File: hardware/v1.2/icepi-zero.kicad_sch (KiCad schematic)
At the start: 29 parts, among them J1 Conn_02x20_Counter_Clockwise, SW1 SW_Push, SW2 SW_Push, U1 ECP5U_25F_CABGA256, Y1 SITxxxxxx-1x-33E-50.000000

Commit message: Trying to document my journey :)
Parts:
- renumbered C25 to C1, C1 to C2, C2 to C3
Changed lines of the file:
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@@
 		(dnp no)
 		(fields_autoplaced yes)
-		(property "Reference" "#PWR013"
+		(property "Reference" "#PWR015"
 			(at 123.19 106.68 0)
 			(effects
@@
 			(project "icepi-zero"
 				(path "/f88da08e-cf42-4d03-a08f-3f602fe6658d"
-					(reference "#PWR013")
+					(reference "#PWR015")
 					(unit 1)
 				)
@@
 		(dnp no)
 		(fields_autoplaced yes)
-		(property "Reference" "#PWR020"
+		(property "Reference" "#PWR022"
 			(at 123.19 144.78 0)
 			(effects
@@
 			(project "icepi-zero"
 				(path "/f88da08e-cf42-4d03-a08f-3f602fe6658d"
-					(reference "#PWR020")
+					(reference "#PWR022")
 					(unit 1)
 				)
@@
 		(dnp no)
 		(fields_autoplaced yes)
-		(property "Reference" "#PWR021"
+		(property "Reference" "#PWR023"
 			(at 223.52 156.21 0)
 			(effects
@@
 			(project ""
 				(path "/f88da08e-cf42-4d03-a08f-3f602fe6658d"
-					(reference "#PWR021")
+					(reference "#PWR023")
 					(unit 1)
 				)
@@
 		(dnp no)
 		(fields_autoplaced yes)
-		(property "Reference" "#PWR016"
+		(property "Reference" "#PWR018"
 			(at 148.59 119.38 0)
 			(effects
@@
 			(project "icepi-zero"
 				(path "/f88da08e-cf42-4d03-a08f-3f602fe6658d"
-					(reference "#PWR016")
+					(reference "#PWR018")
 					(unit 1)
 				)
@@
 		(dnp no)
 		(fields_autoplaced yes)
-		(property "Reference" "#PWR017"
+		(property "Reference" "#PWR019"
 			(at 123.19 127 0)
 			(effects
@@
 			(project "icepi-zero"
 				(path "/f88da08e-cf42-4d03-a08f-3f602fe6658d"
-					(reference "#PWR017")
+					(reference "#PWR019")
 					(unit 1)
 				)
@@
 		(dnp no)
 		(fields_autoplaced yes)
-		(property "Reference" "#PWR011"
+		(property "Reference" "#PWR013"
 			(at 138.43 99.06 0)
 			(effects
@@
 			(project ""
 				(path "/f88da08e-cf42-4d03-a08f-3f602fe6658d"
-					(reference "#PWR011")
+					(reference "#PWR013")
 					(unit 1)
 				)
@@
 		(dnp no)
 		(fields_autoplaced yes)
-		(property "Reference" "#PWR05"
+		(property "Reference" "#PWR07"
 			(at 247.65 62.23 0)
 			(effects
@@
 			(project ""
 				(path "/f88da08e-cf42-4d03-a08f-3f602fe6658d"
-					(reference "#PWR05")
+					(reference "#PWR07")
 					(unit 1)
 				)
@@
 		(dnp no)
 		(fields_autoplaced yes)
-		(property "Reference" "#PWR09"
+		(property "Reference" "#PWR011"
 			(at 133.35 96.52 0)
 			(effects
@@
 			(project ""
 				(path "/f88da08e-cf42-4d03-a08f-3f602fe6658d"
-					(reference "#PWR09")
+					(reference "#PWR011")
 					(unit 1)
 				)
@@
 		(dnp no)
 		(fields_autoplaced yes)
-		(property "Reference" "C1"
+		(property "Reference" "C2"
 			(at 29.21 81.2862 0)
 			(effects
@@
 			(project "icepi-zero"
 				(path "/f88da08e-cf42-4d03-a08f-3f602fe6658d"
-					(reference "C1")
+					(reference "C2")
 					(unit 1)
 				)
@@
 		(dnp no)
 		(fields_autoplaced yes)
-		(property "Reference" "#PWR019"
+		(property "Reference" "#PWR021"
 			(at 148.59 137.16 0)
 			(effects
@@
 			(project "icepi-zero"
 				(path "/f88da08e-cf42-4d03-a08f-3f602fe6658d"
-					(reference "#PWR019")
+					(reference "#PWR021")
 					(unit 1)
 				)
@@
 		(dnp no)
 		(fields_autoplaced yes)
-		(property "Reference" "#PWR044"
+		(property "Reference" "#PWR04"
 			(at 43.18 62.23 0)
 			(effects
@@
 			(project "icepi-zero"
 				(path "/f88da08e-cf42-4d03-a08f-3f602fe6658d"
-					(reference "#PWR044")
+					(reference "#PWR04")
 					(unit 1)
 				)
@@
 		(dnp no)
 		(fields_autoplaced yes)
-		(property "Reference" "#PWR06"
+		(property "Reference" "#PWR08"
 			(at 257.81 62.23 0)
 			(effects
@@
 			(project ""
 				(path "/f88da08e-cf42-4d03-a08f-3f602fe6658d"
-					(reference "#PWR06")
+					(reference "#PWR08")
 					(unit 1)
 				)
@@
 		(dnp no)
 		(fields_autoplaced yes)
-		(property "Reference" "#PWR022"
+		(property "Reference" "#PWR024"
 			(at 142.24 185.42 0)
 			(effects
@@
 			(project ""
 				(path "/f88da08e-cf42-4d03-a08f-3f602fe6658d"
-					(reference "#PWR022")
+					(reference "#PWR024")
 					(unit 1)
 				)
@@
 		(dnp no)
 		(fields_autoplaced yes)
-		(property "Reference" "#PWR043"
+		(property "Reference" "#PWR01"
 			(at 43.18 41.91 0)
 			(effects
@@
 			(project "icepi-zero"
 				(path "/f88da08e-cf42-4d03-a08f-3f602fe6658d"
-					(reference "#PWR043")
+					(reference "#PWR01")
 					(unit 1)
 				)
@@
 		(dnp no)
 		(fields_autoplaced yes)
-		(property "Reference" "#PWR08"
+		(property "Reference" "#PWR010"
 			(at 36.83 92.71 0)
 			(effects
@@
 			(project "icepi-zero"
 				(path "/f88da08e-cf42-4d03-a08f-3f602fe6658d"
-					(reference "#PWR08")
+					(reference "#PWR010")
 					(unit 1)
 				)
@@
 		(dnp no)
 		(fields_autoplaced yes)
-		(property "Reference" "C2"
+		(property "Reference" "C3"
 			(at 39.37 81.2862 0)
 			(effects
@@
 			(project "icepi-zero"
 				(path "/f88da08e-cf42-4d03-a08f-3f602fe6658d"
-					(reference "C2")
+					(reference "C3")
 					(unit 1)
 				)
@@
 		(dnp no)
 		(fields_autoplaced yes)
-		(property "Reference" "#PWR07"
+		(property "Reference" "#PWR09"
 			(at 24.13 81.28 0)
 			(effects
@@
 			(project "icepi-zero"
 				(path "/f88da08e-cf42-4d03-a08f-3f602fe6658d"
-					(reference "#PWR07")
+					(reference "#PWR09")
 					(unit 1)
 				)
@@
 		(dnp no)
 		(fields_autoplaced yes)
-		(property "Reference" "#PWR010"
+		(property "Reference" "#PWR012"
 			(at 138.43 96.52 0)
 			(effects
@@
 			(project "icepi-zero"
 				(path "/f88da08e-cf42-4d03-a08f-3f602fe6658d"
-					(reference "#PWR010")
+					(reference "#PWR012")
 					(unit 1)
 				)
@@
 		(on_board yes)
 		(dnp no)
-		(property "Reference" "C25"
+		(property "Reference" "C1"
 			(at 28.575 45.72 0)
 			(effects
@@
 			(project "icepi-zero"
 				(path "/f88da08e-cf42-4d03-a08f-3f602fe6658d"
-					(reference "C25")
+					(reference "C1")
 					(unit 1)
 				)
@@
 		(dnp no)
 		(fields_autoplaced yes)
-		(property "Reference" "#PWR04"
+		(property "Reference" "#PWR06"
 			(at 236.22 62.23 0)
 			(effects
@@
 			(project ""
 				(path "/f88da08e-cf42-4d03-a08f-3f602fe6658d"
-					(reference "#PWR04")
+					(reference "#PWR06")
 					(unit 1)
 				)
@@
 		(dnp no)
 		(fields_autoplaced yes)
-		(property "Reference" "#PWR01"
+		(property "Reference" "#PWR02"
 			(at 236.22 49.53 0)
 			(effects
@@
 			(project ""
 				(path "/f88da08e-cf42-4d03-a08f-3f602fe6658d"
-					(reference "#PWR01")
+					(reference "#PWR02")
 					(unit 1)
 				)
@@
 		(dnp no)
 		(fields_autoplaced yes)
-		(property "Reference" "#PWR012"
+		(property "Reference" "#PWR014"
 			(at 148.59 101.6 0)
 			(effects
@@
 			(project ""
 				(path "/f88da08e-cf42-4d03-a08f-3f602fe6658d"
-					(reference "#PWR012")
+					(reference "#PWR014")
 					(unit 1)
 				)
@@
 		(dnp no)
 		(fields_autoplaced yes)
-		(property "Reference" "#PWR018"
+		(property "Reference" "#PWR020"
 			(at 148.59 132.08 0)
 			(effects
@@
 			(project "icepi-zero"
 				(path "/f88da08e-cf42-4d03-a08f-3f602fe6658d"
-					(reference "#PWR018")
+					(reference "#PWR020")
 					(unit 1)
 				)
@@
 		(dnp no)
 		(fields_autoplaced yes)
-		(property "Reference" "#PWR02"
+		(property "Reference" "#PWR03"
 			(at 247.65 49.53 0)
 			(effects
@@
 			(project ""
 				(path "/f88da08e-cf42-4d03-a08f-3f602fe6658d"
-					(reference "#PWR02")
+					(reference "#PWR03")
 					(unit 1)
 				)
@@
 		(dnp no)
 		(fields_autoplaced yes)
-		(property "Reference" "#PWR015"
+		(property "Reference" "#PWR017"
 			(at 133.35 116.84 0)
 			(effects
@@
 			(project "icepi-zero"
 				(path "/f88da08e-cf42-4d03-a08f-3f602fe6658d"
-					(reference "#PWR015")
+					(reference "#PWR017")
 					(unit 1)
 				)
@@
 		(dnp no)
 		(fields_autoplaced yes)
-		(property "Reference" "#PWR03"
+		(property "Reference" "#PWR05"
 			(at 226.06 62.23 0)
 			(effects
@@
 			(project ""
 				(path "/f88da08e-cf42-4d03-a08f-3f602fe6658d"
-					(reference "#PWR03")
+					(reference "#PWR05")
 					(unit 1)
 				)
@@
 		(dnp no)
 		(fields_autoplaced yes)
-		(property "Reference" "#PWR014"
+		(property "Reference" "#PWR016"
 			(at 148.59 111.76 0)
 			(effects
@@
 			(project "icepi-zero"
 				(path "/f88da08e-cf42-4d03-a08f-3f602fe6658d"
-					(reference "#PWR014")
+					(reference "#PWR016")
 					(unit 1)
 				)

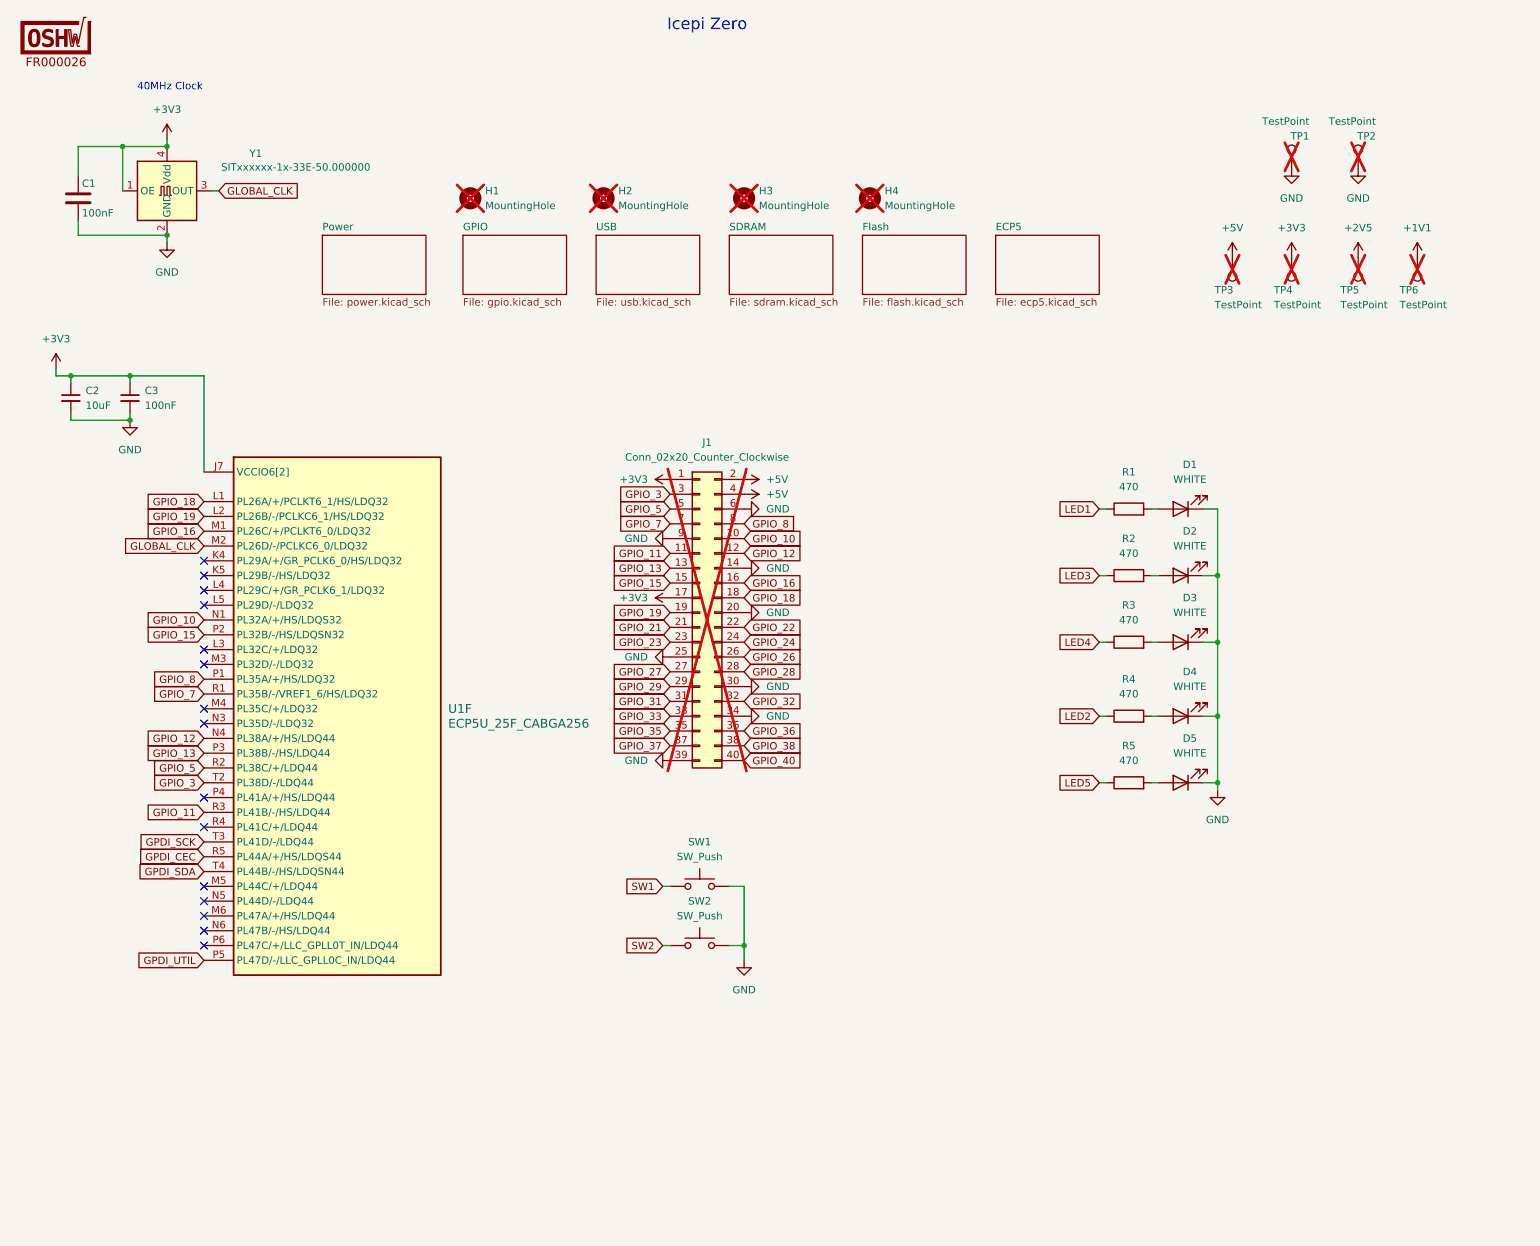
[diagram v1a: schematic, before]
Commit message: Custom ECP5-CABGA256 symbol
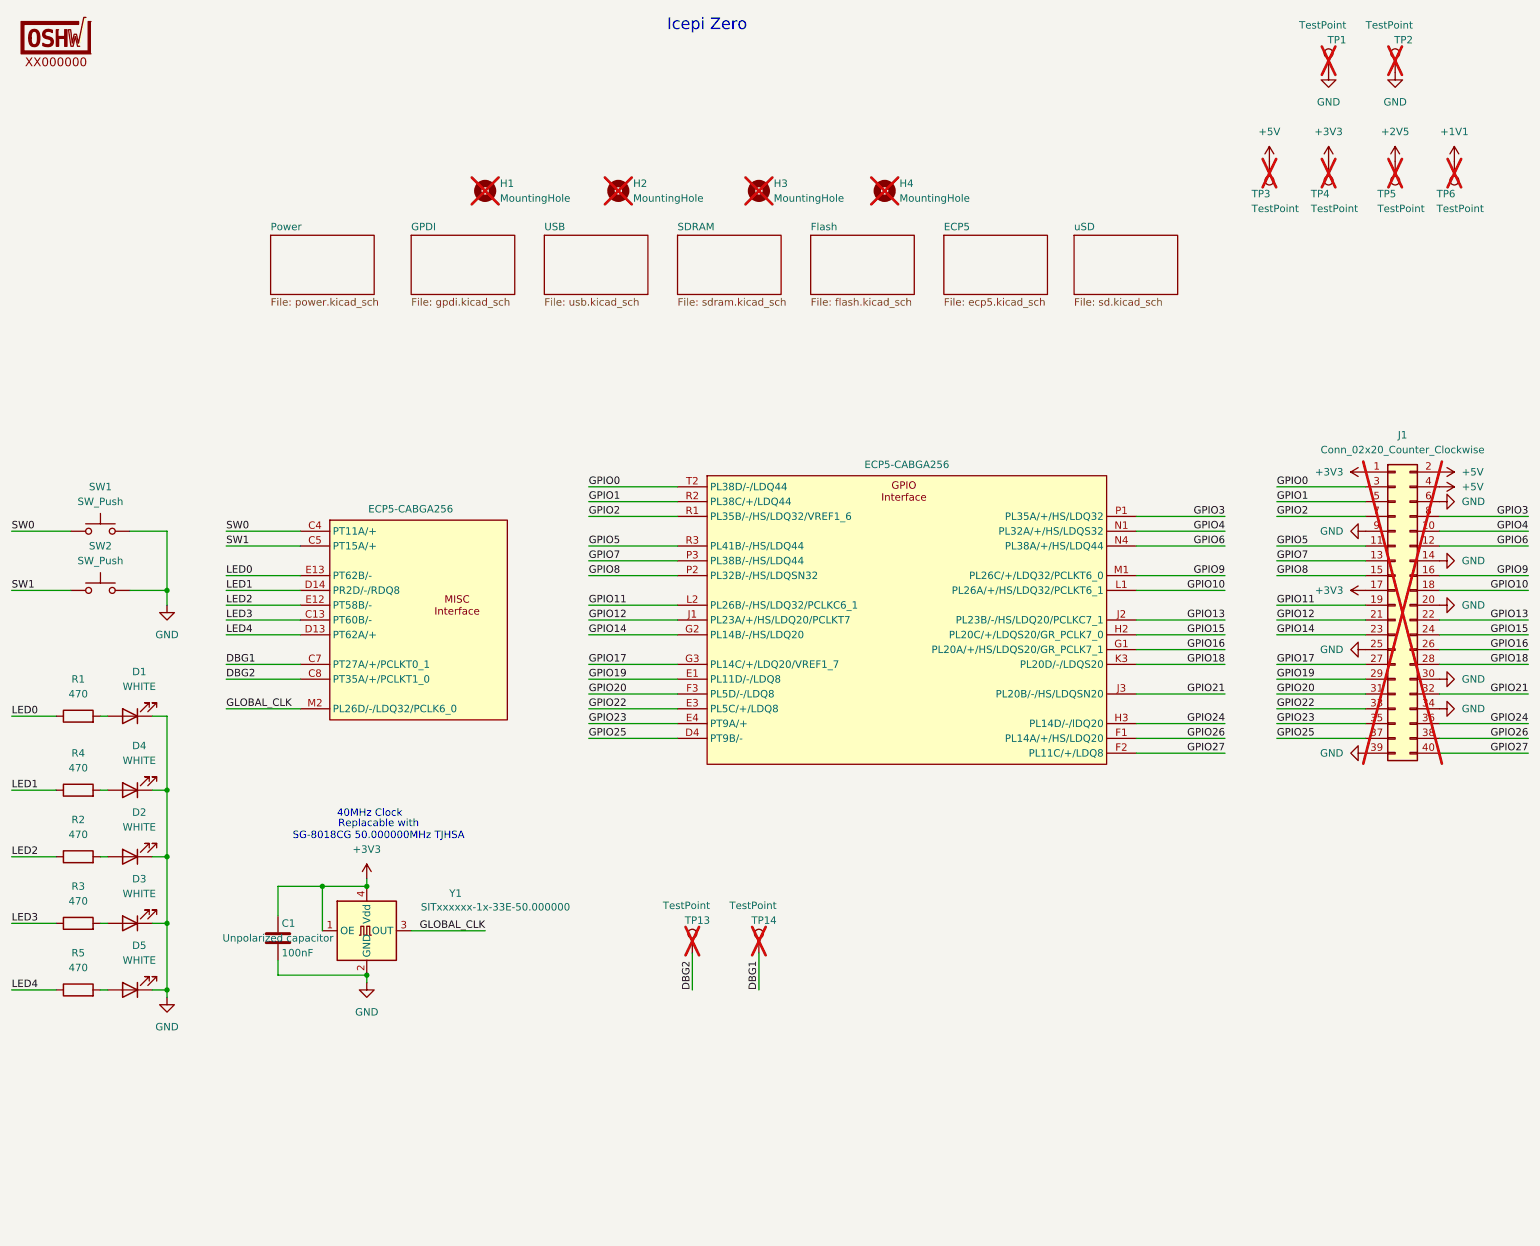
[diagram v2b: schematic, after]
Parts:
- removed C2: 10uF, Capacitor_SMD:C_0603_1608Metric, symbol Device:C_Small
- removed C3: 100nF, Capacitor_SMD:C_0402_1005Metric, symbol Device:C_Small
- removed U1: ECP5U_25F_CABGA256, Package_BGA:BGA-256_14.0x14.0mm_Layout16x16_P0.8mm_Ball0.45mm_Pad0.32mm_NSMD, symbol josh:ECP5U_12_CABGA256
- added TP13, TP14: TestPoint, TestPoint:TestPoint_Pad_D1.0mm, symbol Connector:TestPoint
- added U1: ECP5-CABGA256, Package_BGA:BGA-256_14.0x14.0mm_Layout16x16_P0.8mm_Ball0.45mm_Pad0.32mm_NSMD, symbol icepi-lib:LFE5U-25F-6BG256x
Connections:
- net LED5 is gone; now on net LED4: R5.1
- net SW2 is gone; now on net SW1: SW2.1
- net GLOBAL_CLK: now also U1.M2 (PL26D/-/LDQ32/PCLK6_0)
- net LED1: now also R4.1, U1.D14 (PR2D/-/RDQ8); no longer R1.1
- net LED2: now also R2.1, U1.E12 (PT58B/-); no longer R4.1
- net LED3: now also R3.1, U1.C13 (PT60B/-); no longer R2.1
- net LED4: now also U1.D13 (PT62A/+); no longer R3.1
- net SW1: now also U1.C5 (PT15A/+); no longer SW1.1
- net GPIO_10 renamed GPIO4
- net GPIO4: now also U1.N1 (PL32A/+/HS/LDQS32)
- net GPIO_11 renamed GPIO5
- net GPIO5: now also U1.R3 (PL41B/-/HS/LDQ44)
- net GPIO_12 renamed GPIO6
- net GPIO6: now also U1.N4 (PL38A/+/HS/LDQ44)
- net GPIO_13 renamed GPIO7
- net GPIO7: now also U1.P3 (PL38B/-/HS/LDQ44)
- net GPIO_15 renamed GPIO8
- net GPIO8: now also U1.P2 (PL32B/-/HS/LDQSN32)
- net GPIO_16 renamed GPIO9
- net GPIO9: now also U1.M1 (PL26C/+/LDQ32/PCLKT6_0)
- net GPIO_18 renamed GPIO10
- net GPIO10: now also U1.L1 (PL26A/+/HS/LDQ32/PCLKT6_1)
- net GPIO_19 renamed GPIO11
- net GPIO11: now also U1.L2 (PL26B/-/HS/LDQ32/PCLKC6_1)
- net GPIO_21 renamed GPIO12
- net GPIO12: now also U1.J1 (PL23A/+/HS/LDQ20/PCLKT7)
- net GPIO_22 renamed GPIO13
- net GPIO13: now also U1.J2 (PL23B/-/HS/LDQ20/PCLKC7_1)
- net GPIO_23 renamed GPIO14
- net GPIO14: now also U1.G2 (PL14B/-/HS/LDQ20)
- net GPIO_24 renamed GPIO15
- net GPIO15: now also U1.H2 (PL20C/+/LDQS20/GR_PCLK7_0)
- net GPIO_26 renamed GPIO16
- net GPIO16: now also U1.G1 (PL20A/+/HS/LDQS20/GR_PCLK7_1)
- net GPIO_27 renamed GPIO17
- net GPIO17: now also U1.G3 (PL14C/+/LDQ20/VREF1_7)
- net GPIO_28 renamed GPIO18
- net GPIO18: now also U1.K3 (PL20D/-/LDQS20)
- net GPIO_29 renamed GPIO19
- net GPIO19: now also U1.E1 (PL11D/-/LDQ8)
- net GPIO_3 renamed GPIO0
- net GPIO0: now also U1.T2 (PL38D/-/LDQ44)
- net GPIO_31 renamed GPIO20
- net GPIO20: now also U1.F3 (PL5D/-/LDQ8)
- net GPIO_32 renamed GPIO21
- net GPIO21: now also U1.J3 (PL20B/-/HS/LDQSN20)
- net GPIO_33 renamed GPIO22
- net GPIO22: now also U1.E3 (PL5C/+/LDQ8)
- net GPIO_35 renamed GPIO23
- net GPIO23: now also U1.E4 (PT9A/+)
- net GPIO_36 renamed GPIO24
- net GPIO24: now also U1.H3 (PL14D/-/lDQ20)
- net GPIO_37 renamed GPIO25
- net GPIO25: now also U1.D4 (PT9B/-)
- net GPIO_38 renamed GPIO26
- net GPIO26: now also U1.F1 (PL14A/+/HS/LDQ20)
- net GPIO_40 renamed GPIO27
- net GPIO27: now also U1.F2 (PL11C/+/LDQ8)
- net GPIO_5 renamed GPIO1
- net GPIO1: now also U1.R2 (PL38C/+/LDQ44)
- net GPIO_7 renamed GPIO2
- net GPIO2: now also U1.R1 (PL35B/-/HS/LDQ32/VREF1_6)
- net GPIO_8 renamed GPIO3
- net GPIO3: now also U1.P1 (PL35A/+/HS/LDQ32)
- new net DBG1: TP14.1, U1.C7 (PT27A/+/PCLKT0_1)
- new net DBG2: TP13.1, U1.C8 (PT35A/+/PCLKT1_0)
- new net LED0: R1.1, U1.E13 (PT62B/-)
- new net SW0: SW1.1, U1.C4 (PT11A/+)
- no-connect marks 15 -> 0
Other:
- sheet GPIO renamed GPDI
- added sheet uSD (sd.kicad_sch)
- sheet GPDI: file gpio.kicad_sch -> gpdi.kicad_sch
- note added: "Replacable with SG-8018CG 50.000000MHz TJHSA"
- moved on the sheet: C1, D1, D2, D3, D4, D5, H1, H2, H3, H4, J1, R1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
